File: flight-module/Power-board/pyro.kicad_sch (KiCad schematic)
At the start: 7 parts, among them Q13 Q_PMOS_GDS

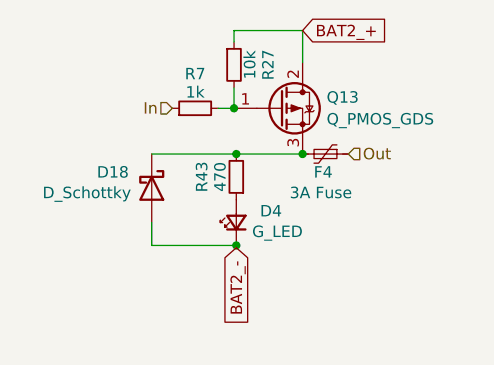
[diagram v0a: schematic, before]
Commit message: Added a gpio expander to power board.
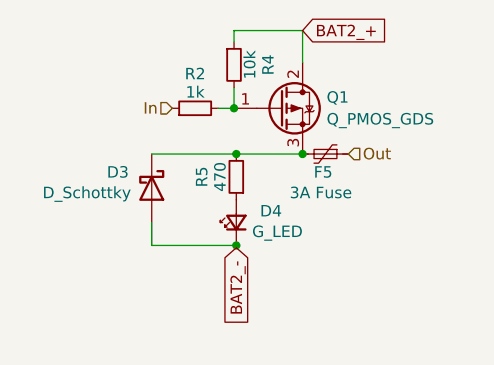
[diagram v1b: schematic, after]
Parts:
- renumbered D18 to D3, F4 to F5, Q13 to Q1, R7 to R2, R27 to R4, R43 to R5
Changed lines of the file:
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@@
   (symbol (lib_id "Device:R_Small") (at 82.55 59.436 180) (unit 1)
     (in_bom yes) (on_board yes) (dnp no)
-    (property "Reference" "R43" (at 78.74 59.436 90)
+    (property "Reference" "R5" (at 78.74 59.436 90)
       (effects (font (size 1.27 1.27)))
     )
@@
   (symbol (lib_id "Device:D_Schottky") (at 73.152 60.706 270) (unit 1)
     (in_bom yes) (on_board yes) (dnp no)
-    (property "Reference" "D18" (at 70.612 58.928 90)
+    (property "Reference" "D3" (at 70.612 58.928 90)
       (effects (font (size 1.27 1.27)) (justify right))
     )
@@
   (symbol (lib_id "Device:Q_PMOS_GDS") (at 87.376 51.816 0) (unit 1)
     (in_bom yes) (on_board yes) (dnp no) (fields_autoplaced)
-    (property "Reference" "Q13" (at 92.583 50.6039 0)
+    (property "Reference" "Q1" (at 92.583 50.6039 0)
       (effects (font (size 1.27 1.27)) (justify left))
     )
@@
   (symbol (lib_id "Device:Polyfuse_Small") (at 92.456 56.896 270) (unit 1)
     (in_bom yes) (on_board yes) (dnp no)
-    (property "Reference" "F4" (at 92.202 58.928 90)
+    (property "Reference" "F5" (at 92.202 58.928 90)
       (effects (font (size 1.27 1.27)))
     )
@@
   (symbol (lib_id "Device:R_Small") (at 82.296 46.99 0) (unit 1)
     (in_bom yes) (on_board yes) (dnp no)
-    (property "Reference" "R27" (at 86.106 46.99 90)
+    (property "Reference" "R4" (at 86.106 46.99 90)
       (effects (font (size 1.27 1.27)))
     )
@@
   (symbol (lib_id "Device:R_Small") (at 77.978 51.816 90) (unit 1)
     (in_bom yes) (on_board yes) (dnp no)
-    (property "Reference" "R7" (at 77.978 48.006 90)
-      (effects (font (size 1.27 1.27)))
-    )
+    (property "Reference" "R2" (at 77.978 48.006 90)
+      (effects (font (size 1.27 1.27)))
+    )

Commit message: power board updated
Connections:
- net BAT2_+ renamed V_pyro_+
- net BAT2_- renamed GND2

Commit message: update on flight pcbs
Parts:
- renumbered D3 to D7, D4 to D8, R5 to R10, R2 to R8, R4 to R9

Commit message: merge conflict fix
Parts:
- renumbered D7 to D3, D8 to D4, R8 to R2, R9 to R4, R10 to R5
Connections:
- net V_pyro_+ renamed SENS_N_PYRO+
